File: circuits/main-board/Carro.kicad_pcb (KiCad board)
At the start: 2 copper layers, 54 x 61 mm, 13 parts, among them J1 Battery, J2 M1-1, J3 LEDs, J4 SR-04, J5 HC-05, J6 CNY70, J7 M1-2, J8 M2-1, J9 M2-2, U1 L293D

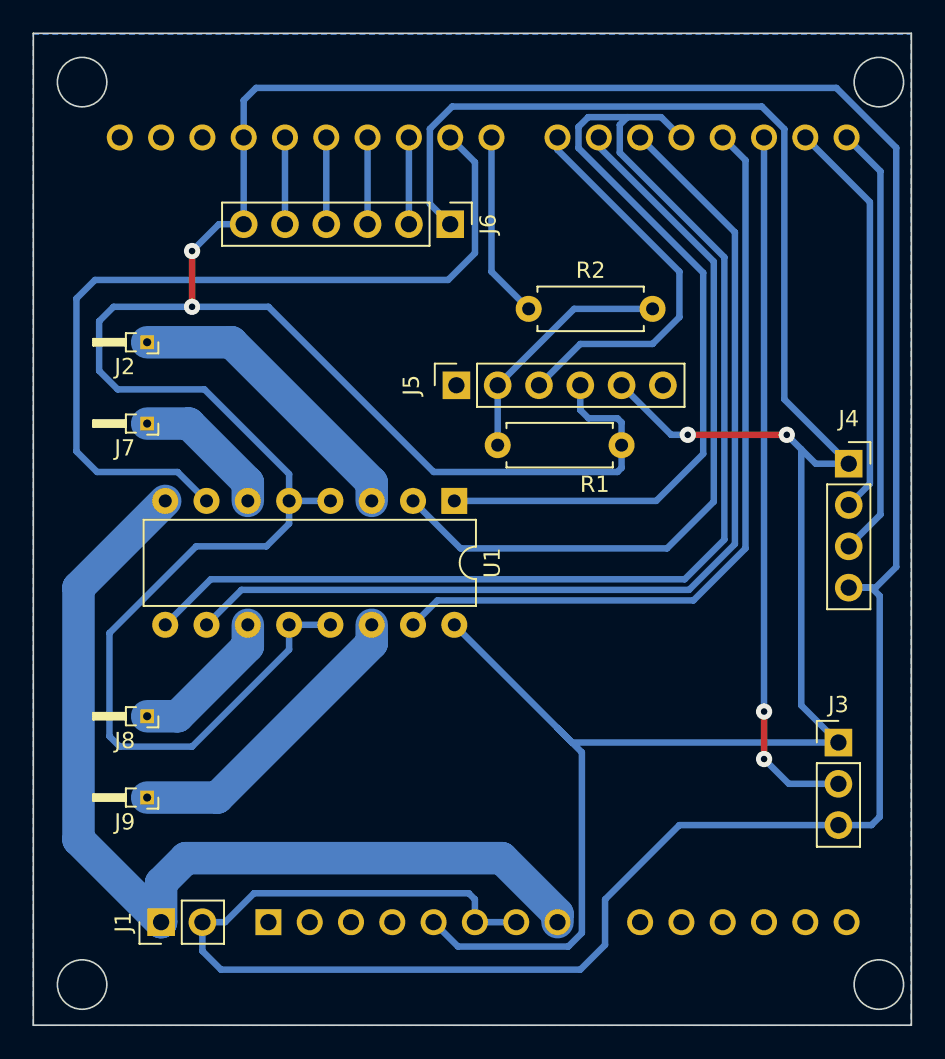
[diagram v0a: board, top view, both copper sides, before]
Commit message: New CNY70 board
Changes in tracks and spacings to match new configuration on CNC.
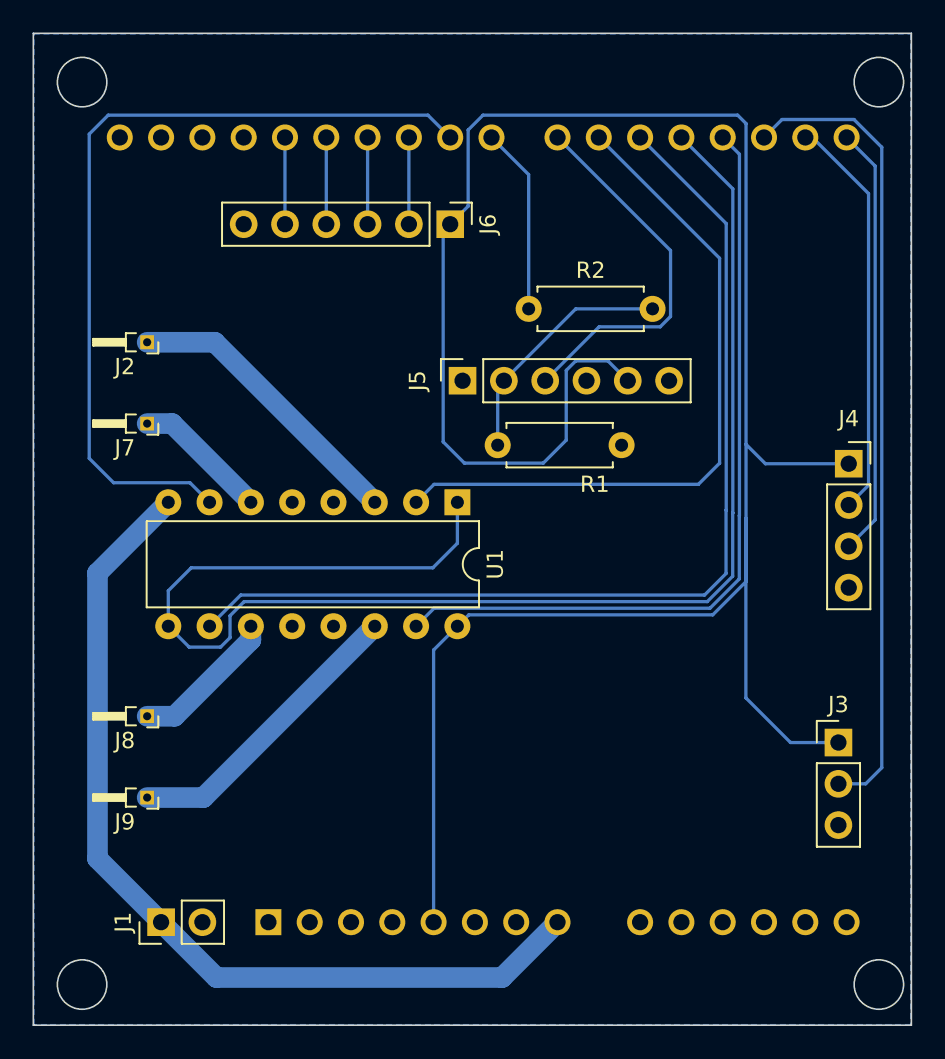
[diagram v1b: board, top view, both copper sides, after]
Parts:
- moved J5 0.47 mm to (144.4, 72.4)
- moved U1 0.21 mm to (144.1, 79.8)
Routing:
- net GND: track 277.8 -> 0.00 mm, vias 2 -> 0
- net /En_M: track 112.3 -> 89.8 mm
- net +5V: track 136.4 -> 145.6 mm, vias 2 -> 0
- net /Din: track 43.4 -> 49.6 mm, vias 2 -> 0
- net /M1_D1: track 46.2 -> 42.8 mm
- net VCC: track 59.6 -> 56.4 mm
- net /TX-HC05: track 24.5 -> 23.2 mm
- net /PM2-2: track 18.9 -> 18.4 mm
